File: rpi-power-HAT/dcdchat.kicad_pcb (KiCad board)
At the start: 2 copper layers, 65 x 56.5 mm, 35 parts, among them J1 Screw_Terminal_01x02, J2 Screw_Terminal_01x02, J3 Conn_01x04_Male, J4 Conn_01x03_Male, J5 Conn_01x04_Male, P1 Conn_02x20_Odd_Even, Q1 SUD50P10-43L, Q2 DMG2305UX, U1 AP64500, U2 DMMT5401

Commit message: Replacing components in PCB editor due to 08.12.2024 message
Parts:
- L1: value 3.6uH -> 4.7uH; footprint Inductor_SMD:L_0805_2012Metric -> YSPI0724-4R7M:IND-SMD_L7.3-W6.6_YSPI07XX
- moved J5 41.7 mm to (157.1, 67.6), turned to 0 degrees
- moved J3 40.1 mm to (168.8, 67.6), turned to 0 degrees
- moved R10 31.9 mm to (155.1, 73.8), turned to 180 degrees
- moved J1 29.8 mm to (141.5, 69.4)
- moved J2 29.2 mm to (141.4, 98.8)
- moved R9 28.4 mm to (158.9, 73.8)
- moved J4 23.5 mm to (180.1, 67.7), turned to 0 degrees
- moved R8 23.1 mm to (153.8, 89.2)
- moved D2 23.0 mm to (150.3, 89.1)
- moved Q1 22.7 mm to (151.4, 96.6)
- moved R2 22.3 mm to (153.2, 105.3)
- moved R1 22.2 mm to (148.5, 105.2)
- moved C1 22.1 mm to (150.7, 105.2)
- moved U1 21.8 mm to (159.3, 100.0)
- moved C3 21.6 mm to (159.2, 94.2)
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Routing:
- net /GPIO3(I2C1_SCL): track 0.00 -> 28.9 mm
- net /GPIO2(I2C1_SDA): track 0.00 -> 27.6 mm
- net /GPIO0(UART1_TX): track 0.00 -> 16.5 mm
- net /GPIO15(UART0_RX): track 0.00 -> 15.2 mm
- net /GPIO14(UART0_TX): track 0.00 -> 13.0 mm
- net VCC: track 0.00 -> 10.7 mm
- net /GPIO5(UART1_RX): track 0.00 -> 10.1 mm
- net Net-(J5-Pad2): track 0.00 -> 6.48 mm
- net Net-(C4-Pad1): track 0.00 -> 5.44 mm
- net Net-(C2-Pad1): track 0.00 -> 2.05 mm

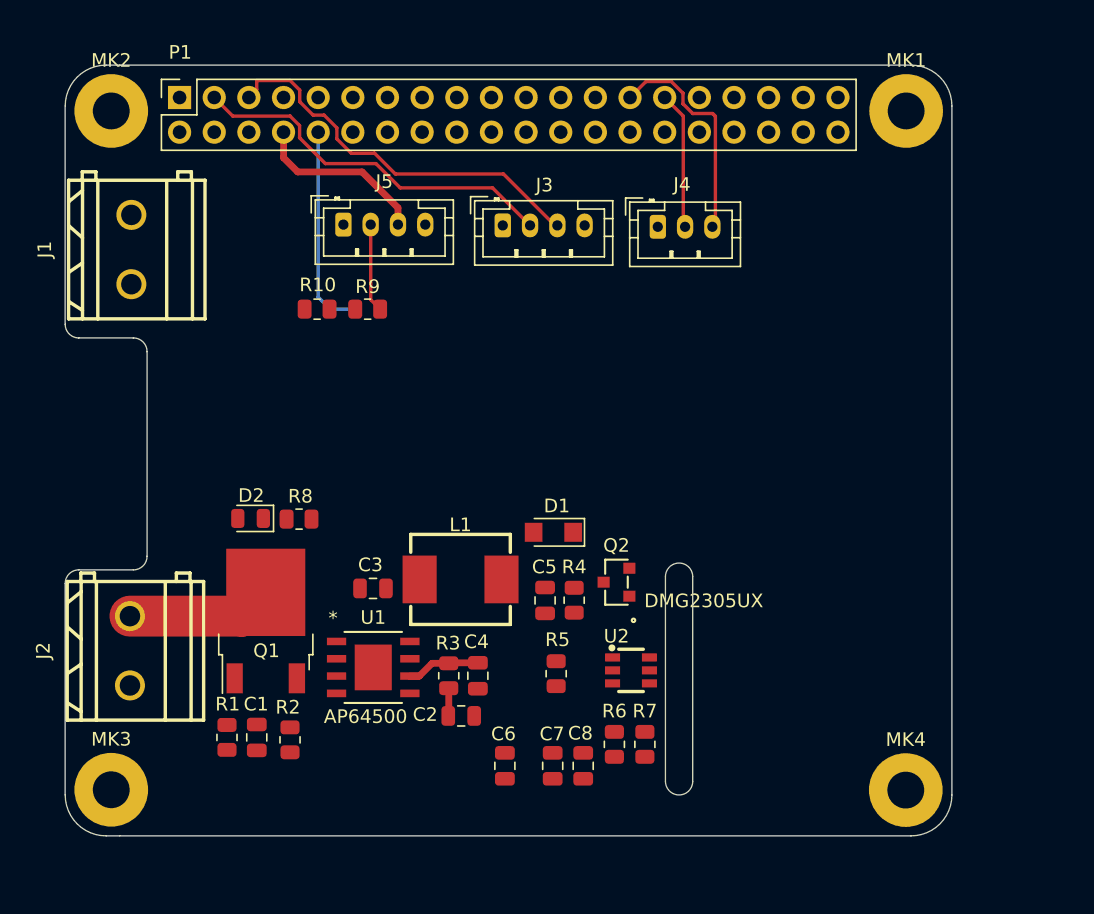
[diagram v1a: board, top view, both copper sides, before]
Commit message: Added polygons between pins. Havent added polygons for GND and output connection yet
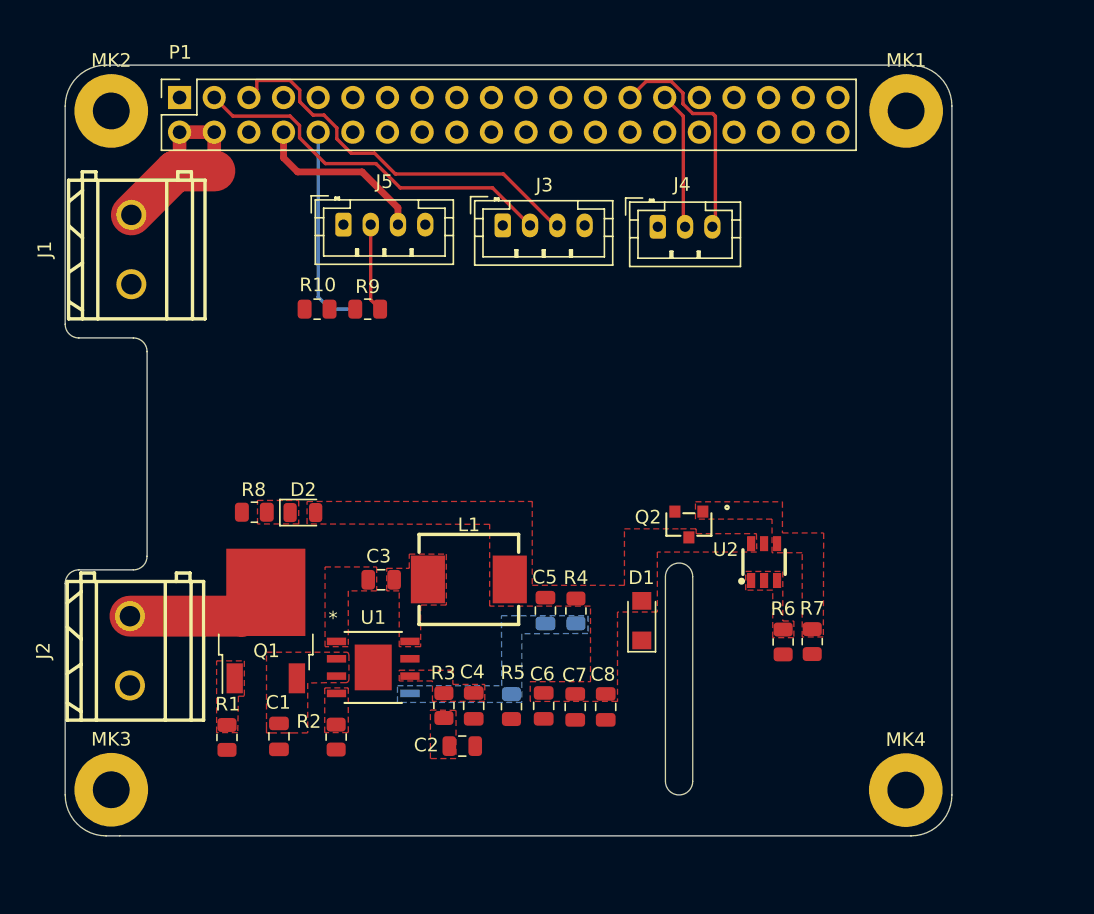
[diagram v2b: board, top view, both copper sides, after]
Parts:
- moved R6 14.5 mm to (189.3, 98.2)
- moved R7 14.4 mm to (191.4, 98.1)
- moved U2 12.6 mm to (187.9, 92.3), turned to -90 degrees
- moved D1 9.16 mm to (178.9, 96.6), turned to 90 degrees
- moved Q2 6.79 mm to (182.4, 89.5), turned to 180 degrees
- moved C6 5.23 mm to (171.8, 102.8)
- moved C7 4.62 mm to (174.1, 102.9)
- moved C8 4.62 mm to (176.3, 102.9)
- moved R5 4.07 mm to (169.4, 102.9)
- moved D2 3.86 mm to (154.1, 88.7), turned to 0 degrees
- moved R2 3.39 mm to (156.5, 105.1)
- moved R8 3.32 mm to (150.5, 88.6), turned to 180 degrees
- moved C4 2.23 mm to (166.6, 102.8)
- moved R3 2.21 mm to (164.4, 102.8)
- moved C2 2.21 mm to (165.8, 105.8)
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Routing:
- net +5V: track 0.00 -> 15.8 mm
- net Net-(C4-Pad1): track 5.44 -> 0.05 mm
- net Net-(C2-Pad1): track 2.05 -> 0.00 mm
- added copper zone on F.Cu, net +5VD
- added copper zone on F.Cu, net Net-(C1-Pad1)
- added copper zone on F.Cu, net Net-(C2-Pad1)
- added copper zone on F.Cu, net Net-(C3-Pad1)
- added copper zone on F.Cu, net Net-(C3-Pad2)
- added copper zone on F.Cu, net Net-(C4-Pad1)
- added copper zone on B.Cu, net Net-(C5-Pad2)
- added copper zone on F.Cu, net Net-(D2-Pad1)
- added copper zone on F.Cu, net Net-(Q1-Pad1)
- added copper zone on F.Cu, net Net-(Q2-Pad1)
- added copper zone on F.Cu, net Net-(R2-Pad1)
- added copper zone on F.Cu, net Net-(R6-Pad2)

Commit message: added traces and polygons on PCB
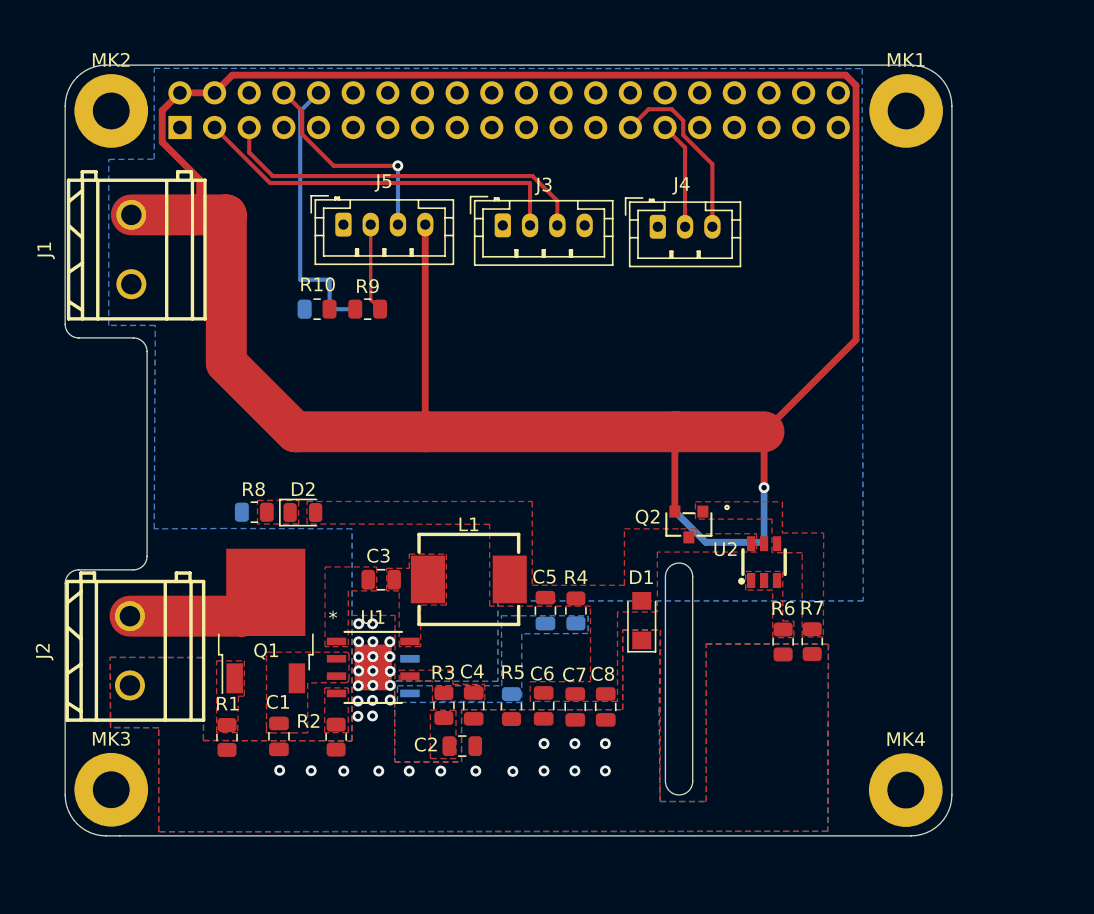
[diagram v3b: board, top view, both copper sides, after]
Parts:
- P1: moved to B.Cu
- moved P1 2.20 mm to (145.1, 60.4), turned to -90 degrees
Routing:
- net +5V: track 15.8 -> 185.4 mm, vias 0 -> 1
- net /GPIO15(UART0_RX): track 15.2 -> 20.4 mm
- net /GPIO14(UART0_TX): track 13.0 -> 15.9 mm, vias 0 -> 1
- net /GPIO0(UART1_TX): track 16.5 -> 13.8 mm
- net /GPIO5(UART1_RX): track 10.1 -> 8.07 mm
- net /GPIO3(I2C1_SCL): track 28.9 -> 27.9 mm
- net GND: track 0.00 -> 0.82 mm, vias 0 -> 33
- added copper zone on B.Cu, net GND
- added copper zone on F.Cu, net GND

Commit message: Finalize the PCB layout
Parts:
- C1, C6, C7, C8: footprint Capacitor_SMD:C_0805_2012Metric -> Capacitor_SMD:C_2220_5750Metric
- C4: value 39.8pF -> 39pF
- C5: value OPEN -> 47pF
- Q1: value SUD50P10-43L -> SUD50P10-43L-TP
- R4: value 119k -> 120k
- moved R7 45.8 mm to (146.3, 90.5)
- moved R6 45.8 mm to (144.2, 90.5)
- moved U2 43.0 mm to (145.4, 86.0), turned to 180 degrees
- moved Q2 32.9 mm to (149.6, 86.3)
- moved D1 29.9 mm to (149.6, 90.9)
- moved R8 28.0 mm to (169.2, 109.5)
- moved D2 27.9 mm to (172.7, 109.5)
- moved C8 24.4 mm to (154.4, 92.2)
- moved R1 17.7 mm to (165.7, 109.5), turned to 0 degrees
- moved C6 15.5 mm to (160.5, 92.2)
- moved R10 14.3 mm to (165.8, 64.2), turned to -90 degrees
- moved J3 13.4 mm to (155.4, 69.0)
- moved R9 13.2 mm to (167.9, 64.2), turned to -90 degrees
- moved C7 13.1 mm to (166.6, 92.2)
- moved C5 11.6 mm to (172.7, 107.4), turned to 180 degrees
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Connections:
- J2 pad 1: GND -> VCC
- J2 pad 2: VCC -> GND
- U1 pad EPAD: (no net) -> GND
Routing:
- net +5V: track 185.4 -> 98.3 mm, vias 1 -> 6
- net +5VD: track 0.00 -> 32.6 mm, vias 0 -> 2
- net +3.3V: track 0.00 -> 19.9 mm
- net /GPIO3(I2C1_SCL): track 27.9 -> 12.8 mm
- net /GPIO2(I2C1_SDA): track 27.9 -> 13.3 mm
- net Net-(U1-SW): track 0.00 -> 13.8 mm, vias 0 -> 2
- net VCC: track 10.7 -> 0.00 mm, vias 0 -> 20
- net GND: track 0.82 -> 9.86 mm, vias 33 -> 21
- net /GPIO14(UART0_TX): track 15.9 -> 24.5 mm, vias 1 -> 0
- net Net-(U2-C2): track 0.00 -> 7.39 mm
- net Net-(U1-FB): track 0.00 -> 5.87 mm
- net Net-(U1-COMP): track 0.05 -> 4.71 mm
- net Net-(Q1-G): track 0.00 -> 4.65 mm
- net Net-(U2-B1): track 0.00 -> 4.60 mm
- net /GPIO15(UART0_RX): track 20.4 -> 16.0 mm
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- added copper zone on B.Cu, net VCC
- added copper zone on F.Cu, net VCC
- removed copper zone on F.Cu, net Net-(C2-Pad1)
- removed copper zone on F.Cu, net Net-(D2-K)
- removed copper zone on F.Cu, net Net-(Q1-G)
- removed copper zone on F.Cu, net Net-(U1-BST)
- removed copper zone on F.Cu, net Net-(U1-COMP)
- removed copper zone on B.Cu, net Net-(U1-FB)
- removed copper zone on F.Cu, net Net-(U1-RT/CLK)
- removed copper zone on F.Cu, net Net-(U1-SW)
- removed copper zone on F.Cu, net Net-(U2-B1)
- removed copper zone on F.Cu, net Net-(U2-C2)
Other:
- board text added: "+"
- board text added: "-"
- board text added: "3.3V"
- board text added: "5V"
- board text added: "GND"
- board text added: "IN 5-40V"
- board text added: "KPI Rover RPI Power HAT Ver. 1.0"
- board text added: "OUT 5V"
- board text added: "RX"
- board text added: "SCL"
- board text added: "SDA"
- board text added: "TX"
